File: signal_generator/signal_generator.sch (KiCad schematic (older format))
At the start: 21 parts, among them J1 DAC_OUT, U1 Digilent_CMOD-S7_25, U2 ADC9765, U3 TL072

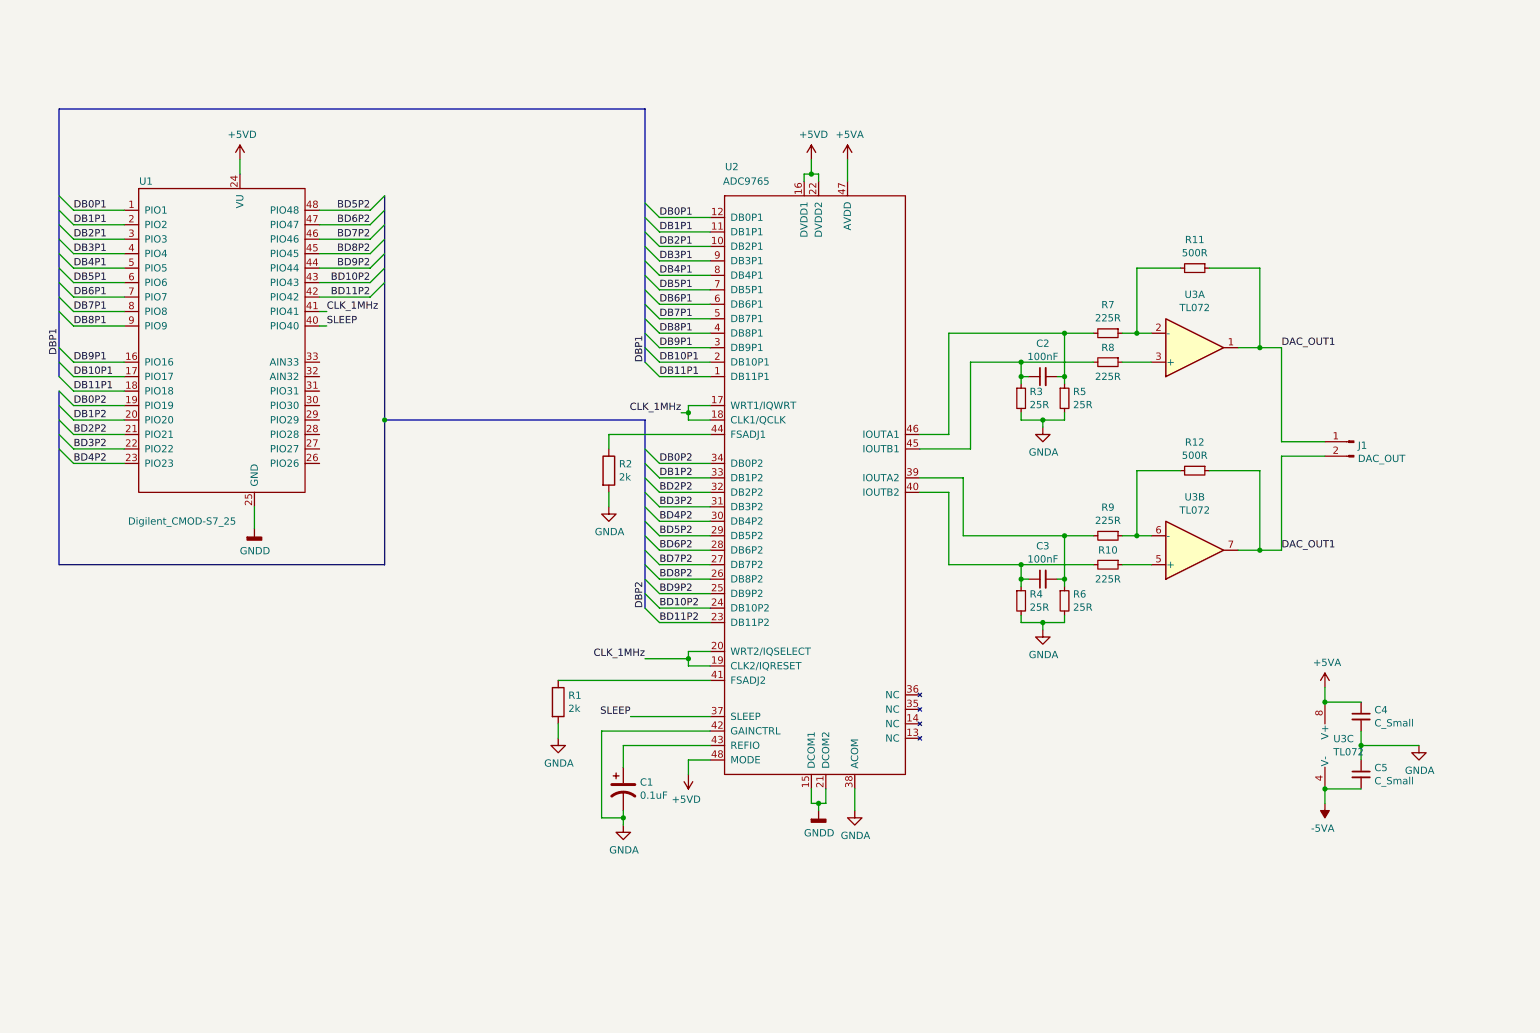
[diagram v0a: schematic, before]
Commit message: new pcb design and pin layout
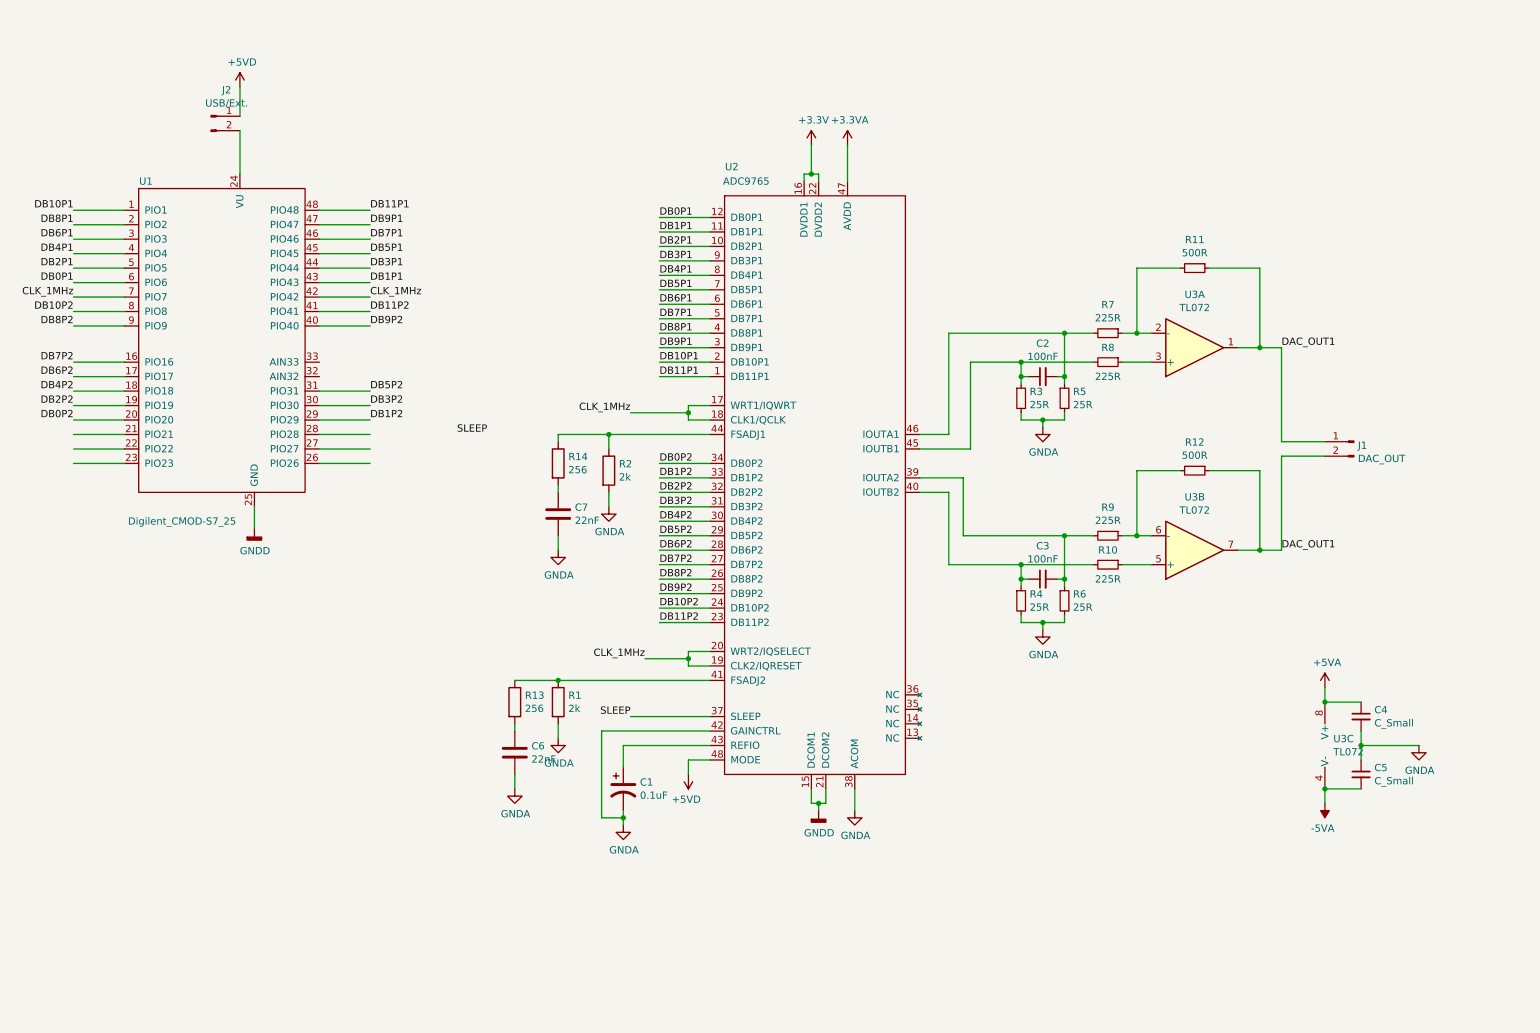
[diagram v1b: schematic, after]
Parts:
- added C6, C7: 22nF, Capacitor_SMD:C_0805_2012Metric, symbol Device:C
- added J2: USB/Ext., Connector_PinSocket_2.54mm:PinSocket_1x02_P2.54mm_Vertical, symbol Connector:Conn_01x02_Male
- added R13, R14: 256, Resistor_SMD:R_0805_2012Metric, symbol Device:R
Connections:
- net labels added: +3.3V, +3.3VA, DB10P2, DB11P2, DB2P2, DB3P2, DB4P2, DB5P2, DB6P2, DB7P2, DB8P2, DB9P2
- net labels removed: BD10P2, BD11P2, BD2P2, BD3P2, BD4P2, BD5P2, BD6P2, BD7P2, BD8P2, BD9P2, DBP1, DBP2
- wire segments 156 -> 170

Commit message: added power supply, integrated in schematic
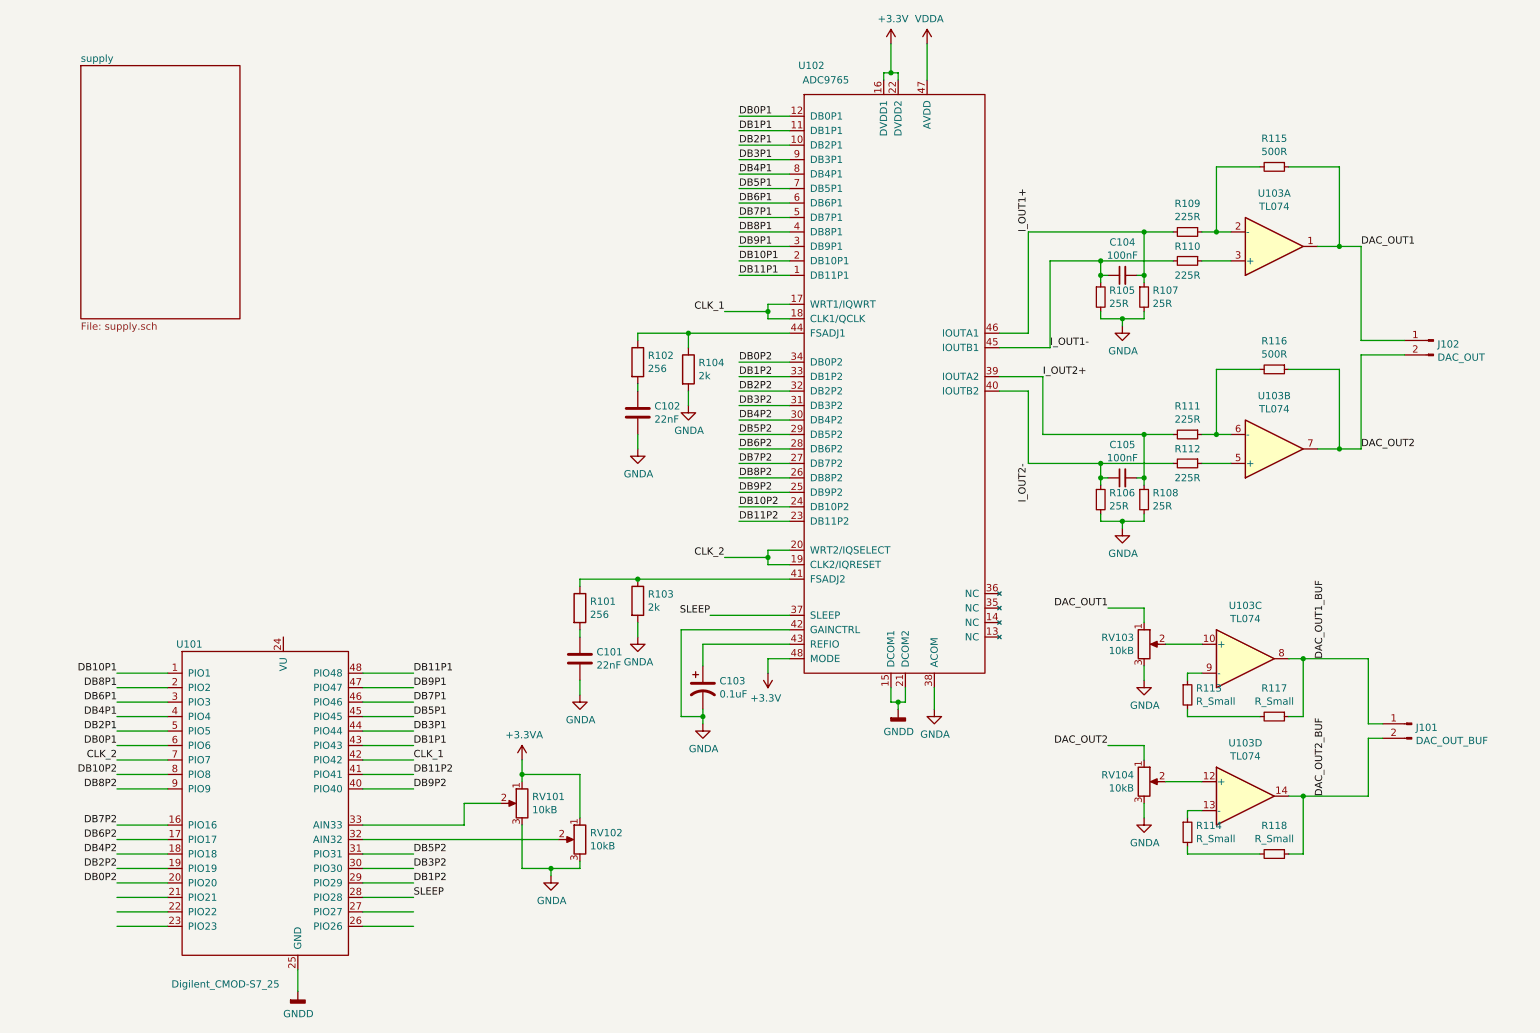
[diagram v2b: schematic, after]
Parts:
- removed C4, C5: C_Small, Capacitor_SMD:C_0805_2012Metric, symbol Device:C_Small
- removed J2: USB/Ext., Connector_PinSocket_2.54mm:PinSocket_1x02_P2.54mm_Vertical, symbol Connector:Conn_01x02_Male
- removed U3: TL072, Package_SO:SOIC-8_3.9x4.9mm_P1.27mm, symbol Amplifier_Operational:TL072
- added J101: DAC_OUT_BUF, Connector_PinHeader_2.54mm:PinHeader_1x02_P2.54mm_Vertical, symbol Connector:Conn_01x02_Male
- added R113, R114, R117, R118: R_Small, Resistor_SMD:R_0603_1608Metric, symbol Device:R_Small
- added RV101, RV102, RV103, RV104: 10kB, Potentiometer_THT:Potentiometer_Alpha_RD901F-40-00D_Single_Vertical_CircularHoles, symbol Device:R_POT
- added U103: TL074, Package_SO:SSOP-14_5.3x6.2mm_P0.65mm, symbol Amplifier_Operational:TL074
- C101: renamed from C6; footprint Capacitor_SMD:C_0805_2012Metric -> Capacitor_SMD:C_0603_1608Metric
- C102: renamed from C7; footprint Capacitor_SMD:C_0805_2012Metric -> Capacitor_SMD:C_0603_1608Metric
- C103: renamed from C1; footprint Capacitor_SMD:CP_Elec_5x5.3 -> DSC-Supply:153CLV-0405
- C104: renamed from C2; footprint Capacitor_SMD:C_0805_2012Metric -> Capacitor_SMD:C_0603_1608Metric
- C105: renamed from C3; footprint Capacitor_SMD:C_0805_2012Metric -> Capacitor_SMD:C_0603_1608Metric
- R101: renamed from R13; footprint Resistor_SMD:R_0805_2012Metric -> Resistor_SMD:R_0603_1608Metric
- R102: renamed from R14; footprint Resistor_SMD:R_0805_2012Metric -> Resistor_SMD:R_0603_1608Metric
- R103: renamed from R1; footprint Resistor_SMD:R_0805_2012Metric -> Resistor_SMD:R_0603_1608Metric
- R104: renamed from R2; footprint Resistor_SMD:R_0805_2012Metric -> Resistor_SMD:R_0603_1608Metric
- R105: renamed from R3; footprint Resistor_SMD:R_0805_2012Metric -> Resistor_SMD:R_0603_1608Metric
- R106: renamed from R4; footprint Resistor_SMD:R_0805_2012Metric -> Resistor_SMD:R_0603_1608Metric
- R107: renamed from R5; footprint Resistor_SMD:R_0805_2012Metric -> Resistor_SMD:R_0603_1608Metric
- R108: renamed from R6; footprint Resistor_SMD:R_0805_2012Metric -> Resistor_SMD:R_0603_1608Metric
- R109: renamed from R7; footprint Resistor_SMD:R_0805_2012Metric -> Resistor_SMD:R_0603_1608Metric
- R110: renamed from R8; footprint Resistor_SMD:R_0805_2012Metric -> Resistor_SMD:R_0603_1608Metric
- R111: renamed from R9; footprint Resistor_SMD:R_0805_2012Metric -> Resistor_SMD:R_0603_1608Metric
- R112: renamed from R10; footprint Resistor_SMD:R_0805_2012Metric -> Resistor_SMD:R_0603_1608Metric
- R115: renamed from R11; footprint Resistor_SMD:R_0805_2012Metric -> Resistor_SMD:R_0603_1608Metric
- R116: renamed from R12; footprint Resistor_SMD:R_0805_2012Metric -> Resistor_SMD:R_0603_1608Metric
- renumbered J1 to J102, U1 to U101, U2 to U102
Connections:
- net labels added: CLK_1, CLK_2, DAC_OUT1_BUF, DAC_OUT2, DAC_OUT2_BUF, I_OUT1+, I_OUT1-, I_OUT2+, I_OUT2-, VDDA
- net labels removed: +5VA, +5VD, -5VA, CLK_1MHz
- wire segments 170 -> 203
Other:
- moved on the sheet: C101, C102, C103, C104, C105, J102, R101, R102, R103, R104, R105, R106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

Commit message: finished PCB v1
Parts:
- C101, C102: footprint Capacitor_SMD:C_0603_1608Metric -> Capacitor_SMD:C_0603_1608Metric_Pad1.08x0.95mm_HandSolder; symbol Device:C -> signal_generator-rescue:C-Device
- C103: footprint DSC-Supply:153CLV-0405 -> Capacitor_SMD:C_0603_1608Metric_Pad1.08x0.95mm_HandSolder; symbol Device:CP1 -> signal_generator-rescue:CP1-Device
- C104, C105: footprint Capacitor_SMD:C_0603_1608Metric -> Capacitor_SMD:C_0603_1608Metric_Pad1.08x0.95mm_HandSolder; symbol Device:C_Small -> signal_generator-rescue:C_Small-Device
- J101, J102: symbol Connector:Conn_01x02_Male -> signal_generator-rescue:Conn_01x02_Male-Connector
- R101, R102, R103, R104: footprint Resistor_SMD:R_0603_1608Metric -> Resistor_SMD:R_0603_1608Metric_Pad0.98x0.95mm_HandSolder; symbol Device:R -> signal_generator-rescue:R-Device
- R105, R106, R107, R108, R109, R110, R111, R112, R113, R114, R115, R116, R117, R118: footprint Resistor_SMD:R_0603_1608Metric -> Resistor_SMD:R_0603_1608Metric_Pad0.98x0.95mm_HandSolder; symbol Device:R_Small -> signal_generator-rescue:R_Small-Device
- RV101, RV102: symbol Device:R_POT -> signal_generator-rescue:R_POT-Device
- RV103, RV104: value 10kB -> 10kA; symbol Device:R_POT -> signal_generator-rescue:R_POT-Device
- U103: footprint Package_SO:SSOP-14_5.3x6.2mm_P0.65mm -> Package_SO:SOIC-14_3.9x8.7mm_P1.27mm; symbol Amplifier_Operational:TL074 -> signal_generator-rescue:TL074-Amplifier_Operational
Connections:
- net +3.3VA is gone; now on net +3V3: RV101.1, RV102.1
- net NC: now reaches U101.21 (PIO21)
- net NC: now also U101.22 (PIO22), U101.23 (PIO23), U101.26 (PIO26), U101.27 (PIO27)
- net +5V: now reaches U101.24 (VU)
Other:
- note added: "+/- 1V"
